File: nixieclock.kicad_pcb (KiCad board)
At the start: 2 copper layers, 33 parts, among them Q1 MMBTA42, Q2 FDS2672CT, U1 UCC3803

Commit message: things happened
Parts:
- added NX1: IN-12A, nixies-us:nixies-us-IN-12, F.Cu at (136.7, 42.7)
- added NX2: IN-12A, nixies-us:nixies-us-IN-12, F.Cu at (156.5, 42.2)
- added NX3: IN-12A, nixies-us:nixies-us-IN-12, F.Cu at (176.5, 42.0)
- added NX4: IN-12A, nixies-us:nixies-us-IN-12, F.Cu at (196.7, 42.0)
- added NX5: IN-12A, nixies-us:nixies-us-IN-12, F.Cu at (216.6, 42.0)
- added NX6: IN-12A, nixies-us:nixies-us-IN-12, F.Cu at (236.6, 42.0)
- moved Q1 50.8 mm to (168.4, 92.7)
- moved L2 50.0 mm to (159.7, 71.3)
- moved R3 49.8 mm to (144.9, 75.0)
- moved R4 49.8 mm to (144.9, 77.5)
- moved R5 49.8 mm to (144.9, 80.0)
- moved R7 49.8 mm to (144.9, 82.5)
- moved R8 49.8 mm to (144.9, 85.0)
- moved C10 49.8 mm to (136.0, 81.2)
- moved C13 49.8 mm to (136.0, 84.2)
- moved C14 49.8 mm to (136.0, 87.2)
- moved C2 49.8 mm to (130.6, 80.1)
- moved C5 49.8 mm to (136.0, 75.2)
- moved C7 49.8 mm to (130.6, 84.3)
- moved C9 49.8 mm to (136.0, 78.2)
- moved D2 49.8 mm to (173.2, 75.0)
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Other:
- board outline added: 135 x 79.8 mm
- copper layers 2 -> 11

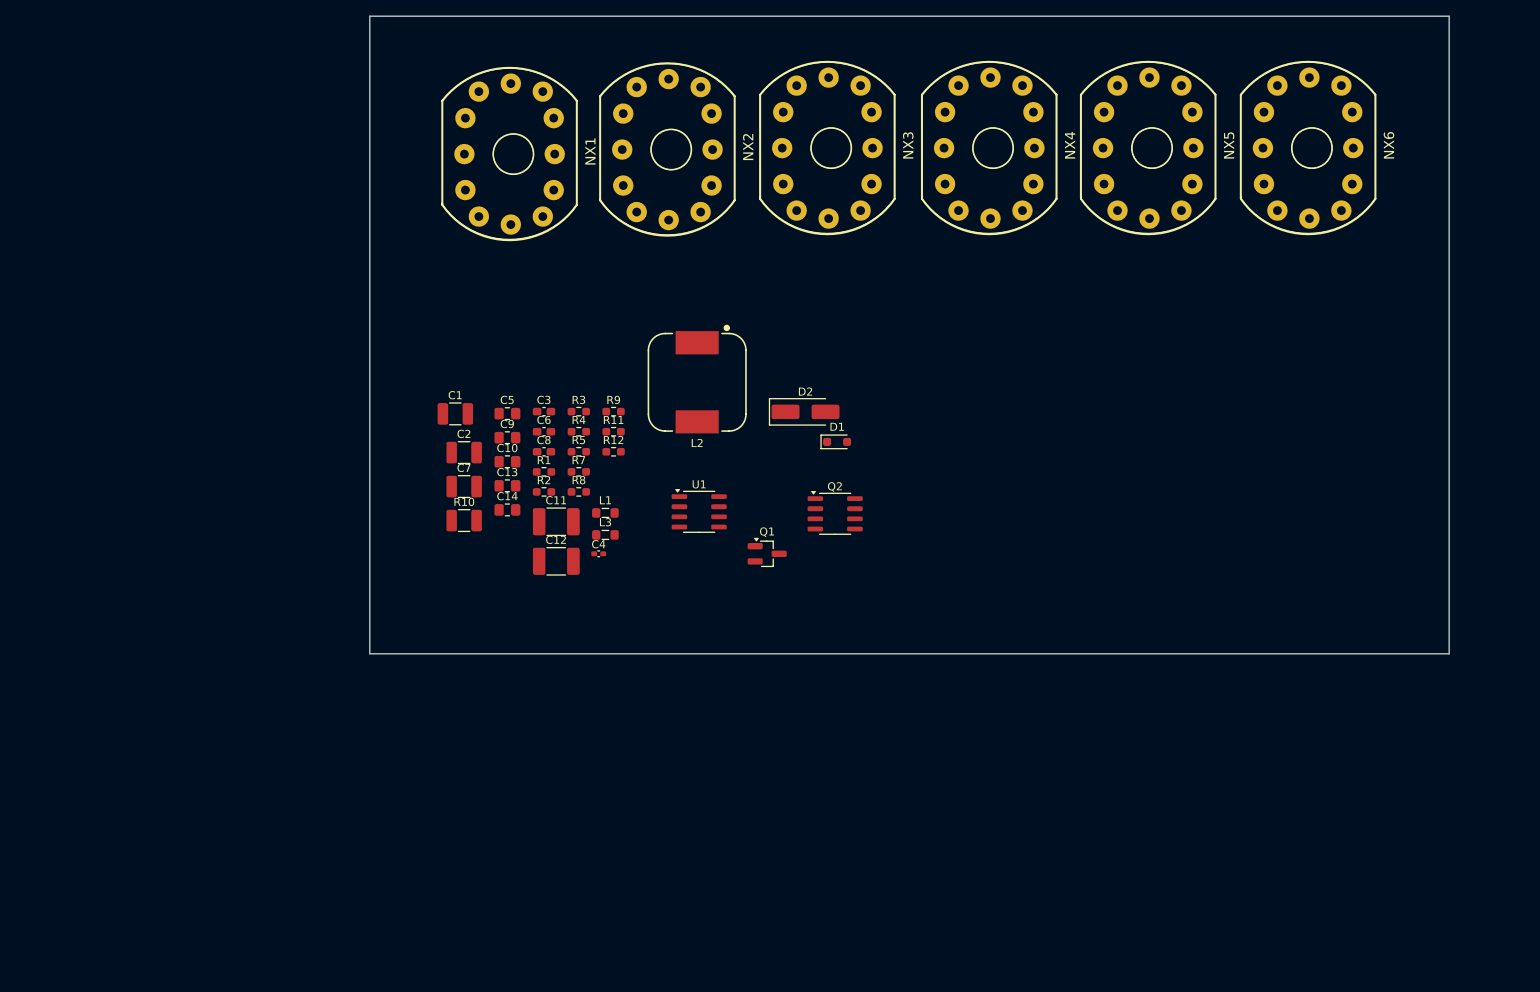
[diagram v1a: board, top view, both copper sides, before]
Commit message: schematic mostly done, started laying out board
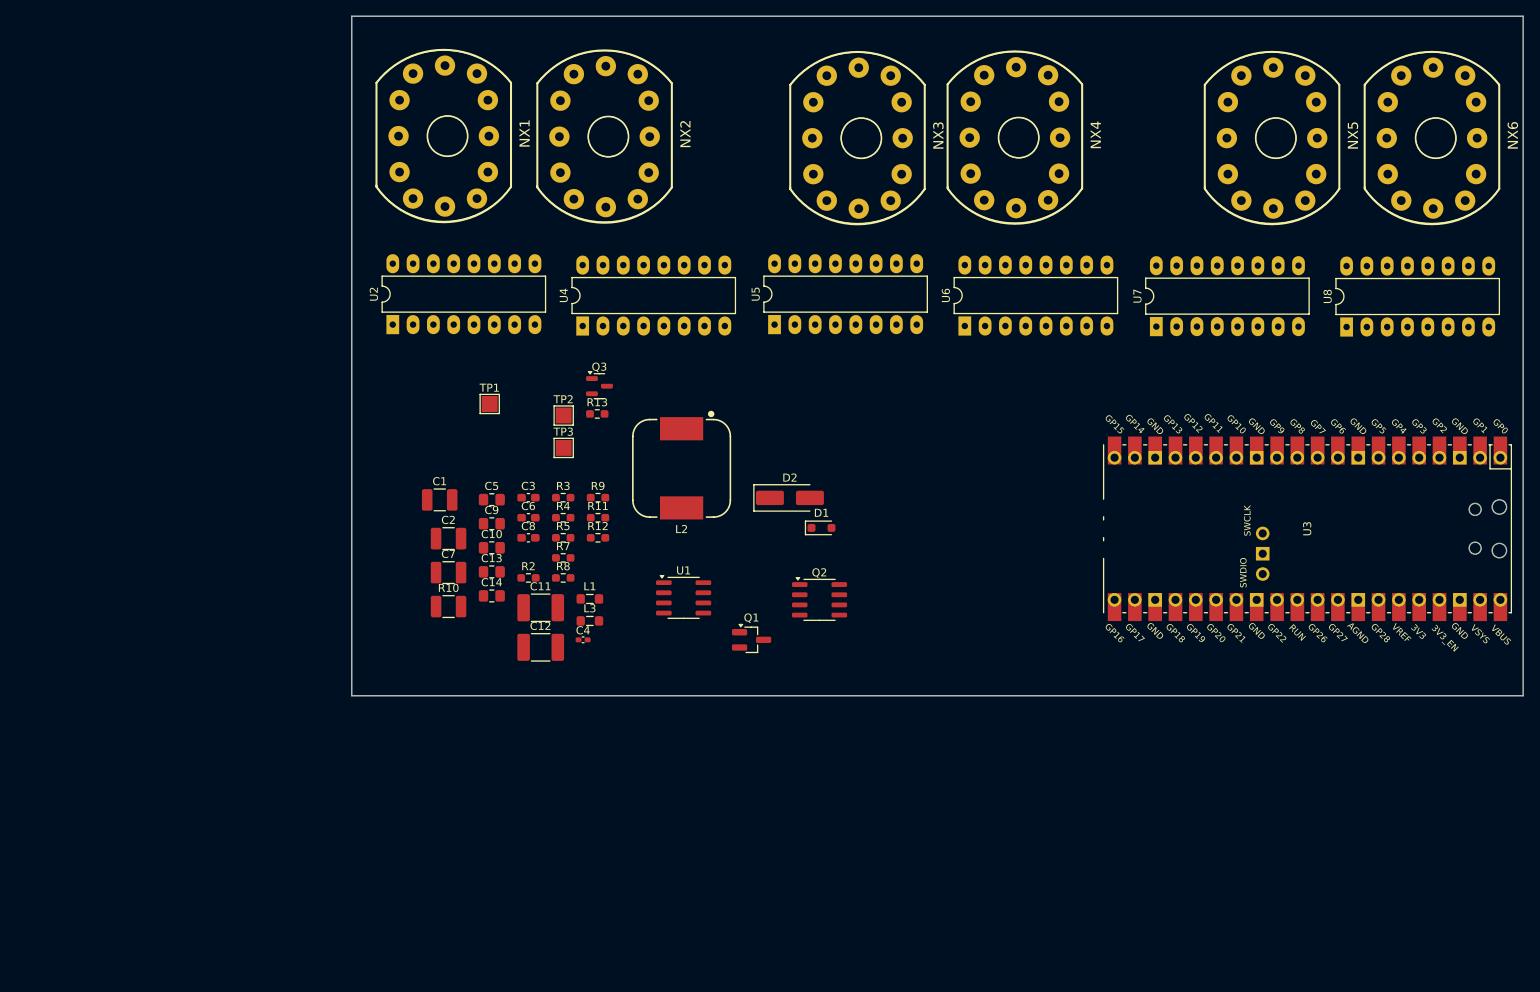
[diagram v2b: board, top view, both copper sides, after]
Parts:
- removed R1: 1k, Resistor_SMD:R_0603_1608Metric_Pad0.98x0.95mm_HandSolder
- added Q3: SS8050, Package_TO_SOT_SMD:SOT-23, F.Cu at (147.5, 71.8)
- added R13: 1k, Resistor_SMD:R_0603_1608Metric_Pad0.98x0.95mm_HandSolder, F.Cu at (147.2, 75.2)
- added TP1: TestPoint_Probe, TestPoint:TestPoint_Pad_2.0x2.0mm, F.Cu at (133.8, 74.0)
- added TP2: TestPoint_Probe, TestPoint:TestPoint_Pad_2.0x2.0mm, F.Cu at (143.0, 75.5)
- added TP3: TestPoint_Probe, TestPoint:TestPoint_Pad_2.0x2.0mm, F.Cu at (143.0, 79.5)
- added U2: K155NA1, Package_DIP:DIP-16_W7.62mm_LongPads, F.Cu at (121.6, 64.1)
- added U3: PicoW, RPi_Pico:RPi_PicoW_SMD_TH, F.Cu at (236.0, 89.6)
- added U4: K155NA1, Package_DIP:DIP-16_W7.62mm_LongPads, F.Cu at (145.4, 64.2)
- added U5: K155NA1, Package_DIP:DIP-16_W7.62mm_LongPads, F.Cu at (169.4, 64.1)
- added U6: K155NA1, Package_DIP:DIP-16_W7.62mm_LongPads, F.Cu at (193.2, 64.2)
- added U7: K155NA1, Package_DIP:DIP-16_W7.62mm_LongPads, F.Cu at (217.1, 64.3)
- added U8: K155NA1, Package_DIP:DIP-16_W7.62mm_LongPads, F.Cu at (240.9, 64.4)
- moved NX5 15.5 mm to (232.1, 40.8)
- moved NX6 15.5 mm to (252.1, 40.8)
- moved C13 10.9 mm to (134.0, 95.0)
- moved C14 10.9 mm to (134.0, 98.0)
- moved C2 10.9 mm to (128.6, 90.8)
- moved C5 10.9 mm to (134.0, 86.0)
- moved C7 10.9 mm to (128.6, 95.1)
- moved C9 10.9 mm to (134.0, 89.0)
- moved R10 10.9 mm to (128.6, 99.3)
- moved R11 10.9 mm to (147.3, 88.2)
- moved R3 10.9 mm to (142.9, 85.7)
- moved R4 10.9 mm to (142.9, 88.2)
- moved R7 10.9 mm to (142.9, 93.2)
- moved R8 10.9 mm to (142.9, 95.8)
- moved R9 10.9 mm to (147.3, 85.7)
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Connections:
- net +160V renamed +170V
- NX1 pad 0: unconnected-(NX1-Pad0) -> Net-(U2-0)
- NX1 pad 1: unconnected-(NX1-Pad1) -> Net-(U2-1)
- NX1 pad 2: unconnected-(NX1-Pad2) -> Net-(U2-2)
- NX1 pad 3: unconnected-(NX1-Pad3) -> Net-(U2-3)
- NX1 pad 4: unconnected-(NX1-Pad4) -> Net-(U2-4)
- NX1 pad 5: unconnected-(NX1-Pad5) -> Net-(U2-5)
- NX1 pad 6: unconnected-(NX1-Pad6) -> Net-(U2-6)
- NX1 pad 7: unconnected-(NX1-Pad7) -> Net-(U2-7)
- NX1 pad 8: unconnected-(NX1-Pad8) -> Net-(U2-8)
- NX1 pad 9: unconnected-(NX1-Pad9) -> Net-(U2-9)
- NX2 pad 0: unconnected-(NX2-Pad0) -> Net-(U4-0)
- NX2 pad 1: unconnected-(NX2-Pad1) -> Net-(U4-1)
- NX2 pad 2: unconnected-(NX2-Pad2) -> Net-(U4-2)
- NX2 pad 3: unconnected-(NX2-Pad3) -> Net-(U4-3)
- NX2 pad 4: unconnected-(NX2-Pad4) -> Net-(U4-4)
- NX2 pad 5: unconnected-(NX2-Pad5) -> Net-(U4-5)
- NX2 pad 6: unconnected-(NX2-Pad6) -> Net-(U4-6)
- NX2 pad 7: unconnected-(NX2-Pad7) -> Net-(U4-7)
- NX2 pad 8: unconnected-(NX2-Pad8) -> Net-(U4-8)
- NX2 pad 9: unconnected-(NX2-Pad9) -> Net-(U4-9)
- NX3 pad 0: unconnected-(NX3-Pad0) -> Net-(U5-0)
- NX3 pad 1: unconnected-(NX3-Pad1) -> Net-(U5-1)
- NX3 pad 2: unconnected-(NX3-Pad2) -> Net-(U5-2)
- NX3 pad 3: unconnected-(NX3-Pad3) -> Net-(U5-3)
- NX3 pad 4: unconnected-(NX3-Pad4) -> Net-(U5-4)
- NX3 pad 5: unconnected-(NX3-Pad5) -> Net-(U5-5)
- NX3 pad 6: unconnected-(NX3-Pad6) -> Net-(U5-6)
- NX3 pad 7: unconnected-(NX3-Pad7) -> Net-(U5-7)
- NX3 pad 8: unconnected-(NX3-Pad8) -> Net-(U5-8)
- NX3 pad 9: unconnected-(NX3-Pad9) -> Net-(U5-9)
- NX4 pad 0: unconnected-(NX4-Pad0) -> Net-(U6-0)
- NX4 pad 1: unconnected-(NX4-Pad1) -> Net-(U6-1)
- NX4 pad 2: unconnected-(NX4-Pad2) -> Net-(U6-2)
- NX4 pad 3: unconnected-(NX4-Pad3) -> Net-(U6-3)
- NX4 pad 4: unconnected-(NX4-Pad4) -> Net-(U6-4)
- NX4 pad 5: unconnected-(NX4-Pad5) -> Net-(U6-5)
- NX4 pad 6: unconnected-(NX4-Pad6) -> Net-(U6-6)
- NX4 pad 7: unconnected-(NX4-Pad7) -> Net-(U6-7)
- NX4 pad 8: unconnected-(NX4-Pad8) -> Net-(U6-8)
- NX4 pad 9: unconnected-(NX4-Pad9) -> Net-(U6-9)
- NX5 pad 0: unconnected-(NX5-Pad0) -> Net-(U7-0)
- NX5 pad 1: unconnected-(NX5-Pad1) -> Net-(U7-1)
- NX5 pad 2: unconnected-(NX5-Pad2) -> Net-(U7-2)
- NX5 pad 3: unconnected-(NX5-Pad3) -> Net-(U7-3)
- NX5 pad 4: unconnected-(NX5-Pad4) -> Net-(U7-4)
- NX5 pad 5: unconnected-(NX5-Pad5) -> Net-(U7-5)
- NX5 pad 6: unconnected-(NX5-Pad6) -> Net-(U7-6)
- NX5 pad 7: unconnected-(NX5-Pad7) -> Net-(U7-7)
- NX5 pad 8: unconnected-(NX5-Pad8) -> Net-(U7-8)
- NX5 pad 9: unconnected-(NX5-Pad9) -> Net-(U7-9)
- NX6 pad 0: unconnected-(NX6-Pad0) -> Net-(U8-0)
- NX6 pad 1: unconnected-(NX6-Pad1) -> Net-(U8-1)
- NX6 pad 2: unconnected-(NX6-Pad2) -> Net-(U8-2)
- NX6 pad 3: unconnected-(NX6-Pad3) -> Net-(U8-3)
- NX6 pad 4: unconnected-(NX6-Pad4) -> Net-(U8-4)
- NX6 pad 5: unconnected-(NX6-Pad5) -> Net-(U8-5)
- NX6 pad 6: unconnected-(NX6-Pad6) -> Net-(U8-6)
- NX6 pad 7: unconnected-(NX6-Pad7) -> Net-(U8-7)
- NX6 pad 8: unconnected-(NX6-Pad8) -> Net-(U8-8)
- NX6 pad 9: unconnected-(NX6-Pad9) -> Net-(U8-9)
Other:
- board size 135 x 79.8 mm -> 146.5 x 85 mm

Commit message: layout
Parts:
- moved D1 42.3 mm to (133.0, 90.0)
- moved Q3 37.1 mm to (129.9, 104.5)
- moved Q1 37.1 mm to (129.8, 98.8), turned to 180 degrees
- moved R13 34.8 mm to (125.5, 102.5), turned to 180 degrees
- moved C11 33.3 mm to (171.8, 89.0), turned to 90 degrees
- moved C13 31.9 mm to (165.8, 98.5), turned to -90 degrees
- moved C12 31.8 mm to (170.8, 96.0), turned to -90 degrees
- moved C9 28.5 mm to (162.5, 89.8)
- moved C7 28.1 mm to (153.2, 81.6), turned to 90 degrees
- moved R10 26.5 mm to (155.0, 96.8), turned to -90 degrees
- moved C10 26.5 mm to (160.2, 95.5), turned to 90 degrees
- moved C14 25.2 mm to (159.0, 101.0), turned to -90 degrees
- moved TP2 23.2 mm to (120.2, 70.7)
- moved TP3 23.2 mm to (120.2, 75.0)
- moved Q2 20.8 mm to (156.2, 89.5), turned to 90 degrees
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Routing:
- net Net-(U1-FB): track 0.00 -> 41.9 mm
- net Net-(D2-A): track 0.00 -> 41.3 mm
- net Net-(U1-Isense): track 0.00 -> 29.0 mm
- net Net-(D2-K): track 0.00 -> 26.1 mm
- net Net-(U1-Vcc): track 0.00 -> 26.0 mm, vias 0 -> 2
- net +5V: track 0.00 -> 18.9 mm
- net Net-(D1-K): track 0.00 -> 15.9 mm
- net Net-(D1-A): track 0.00 -> 15.4 mm
- net Net-(Q2-G): track 0.00 -> 15.2 mm, vias 0 -> 2
- net Net-(U1-Vref): track 0.00 -> 14.3 mm
- net Net-(Q2-S-Pad1): track 0.00 -> 12.2 mm
- net Net-(Q1-B): track 0.00 -> 11.1 mm
- net Net-(U1-R/C): track 0.00 -> 5.63 mm
- net +170V: track 0.00 -> 3.88 mm
- net Net-(Q3-B): track 0.00 -> 3.00 mm
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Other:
- board text added: "+170V"
- board text added: "+5V"
- board text added: "GND"

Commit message: mostly done i guess?
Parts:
- added R1: 10.5k, Resistor_SMD:R_0805_2012Metric_Pad1.20x1.40mm_HandSolder, F.Cu at (100.3, 59.5)
- added R14: 10.5k, Resistor_SMD:R_0805_2012Metric_Pad1.20x1.40mm_HandSolder, F.Cu at (120.1, 59.8)
- added R15: 10.5k, Resistor_SMD:R_0805_2012Metric_Pad1.20x1.40mm_HandSolder, F.Cu at (151.6, 59.8)
- added R16: 10.5k, Resistor_SMD:R_0805_2012Metric_Pad1.20x1.40mm_HandSolder, F.Cu at (171.3, 59.8)
- added R17: 10.5k, Resistor_SMD:R_0805_2012Metric_Pad1.20x1.40mm_HandSolder, F.Cu at (203.3, 60.0)
- added R18: 10.5k, Resistor_SMD:R_0805_2012Metric_Pad1.20x1.40mm_HandSolder, F.Cu at (222.3, 60.0)
- R11, R12: footprint Resistor_SMD:R_0603_1608Metric_Pad0.98x0.95mm_HandSolder -> Resistor_SMD:R_1206_3216Metric_Pad1.30x1.75mm_HandSolder
- moved U3 50.6 mm to (197.2, 118.7)
- moved U4 50.3 mm to (105.2, 94.6)
- moved C1 50.3 mm to (90.1, 125.7)
- moved C10 50.3 mm to (121.3, 127.4)
- moved C2 50.3 mm to (85.3, 121.9)
- moved C3 50.3 mm to (81.6, 121.6)
- moved C6 50.3 mm to (110.3, 129.8)
- moved C7 50.3 mm to (114.3, 113.5)
- moved C9 50.3 mm to (123.6, 121.7)
- moved D1 50.3 mm to (94.1, 121.9)
- moved D2 50.3 mm to (125.6, 116.9)
- moved L1 50.3 mm to (118.1, 113.9)
- moved L2 50.3 mm to (104.1, 118.2)
- moved Q2 50.3 mm to (117.3, 121.4)
- moved Q3 50.3 mm to (91.0, 136.4)
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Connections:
- NX1 pad A: unconnected-(NX1-PadA) -> Net-(NX1-PadA)
- NX2 pad A: unconnected-(NX2-PadA) -> Net-(NX2-PadA)
- NX3 pad A: unconnected-(NX3-PadA) -> Net-(NX3-PadA)
- NX4 pad A: unconnected-(NX4-PadA) -> Net-(NX4-PadA)
- NX5 pad A: unconnected-(NX5-PadA) -> Net-(NX5-PadA)
- NX6 pad A: unconnected-(NX6-PadA) -> Net-(NX6-PadA)
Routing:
- net +170V: track 3.88 -> 281.0 mm
- net +5V: track 18.9 -> 258.2 mm, vias 0 -> 1
- net GPIO0: track 0.00 -> 169.0 mm, vias 0 -> 1
- net GPIO1: track 0.00 -> 146.7 mm, vias 0 -> 1
- net GPIO4: track 0.00 -> 131.1 mm
- net GPIO3: track 0.00 -> 129.7 mm, vias 0 -> 1
- net GPIO2: track 0.00 -> 129.6 mm, vias 0 -> 1
- net GPIO5: track 0.00 -> 111.0 mm, vias 0 -> 1
- net GPIO8: track 0.00 -> 101.3 mm, vias 0 -> 1
- net GPIO6: track 0.00 -> 95.7 mm, vias 0 -> 1
- net GPIO7: track 0.00 -> 90.9 mm, vias 0 -> 1
- net GPIO9: track 0.00 -> 72.5 mm, vias 0 -> 1
- net GPIO12: track 0.00 -> 59.6 mm, vias 0 -> 1
- net GPIO10: track 0.00 -> 56.0 mm, vias 0 -> 1
- net GPIO11: track 0.00 -> 53.5 mm, vias 0 -> 1
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- added copper zone on F.Cu, net GND
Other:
- board text added: "Designed by Alex Park"
- board text added: "High Voltage"
- board text added: "Warning"

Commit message: Finishing touches to pcb
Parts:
- R18: value 10.5k -> R18
- moved Q3 1.86 mm to (91.2, 134.6)
- moved C3 1.16 mm to (82.8, 121.5)
- moved C8 1.01 mm to (98.0, 132.0)
- moved R8 1.01 mm to (105.0, 135.2)
- moved C10 0.85 mm to (120.5, 127.4)
- moved C11 0.79 mm to (133.5, 120.5)
- moved NX1 0.52 mm to (91.0, 71.3)
- moved NX5 0.42 mm to (193.8, 71.3)
- moved NX6 0.42 mm to (213.8, 71.3)
- moved NX2 0.36 mm to (111.0, 71.3)
- moved NX4 0.25 mm to (162.2, 71.3)
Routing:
- net GND: track 0.00 -> 61.5 mm, vias 0 -> 9
- net Net-(U4-4): track 44.8 -> 28.2 mm
- net Net-(D2-K): track 28.6 -> 36.6 mm
- net Net-(U5-7): track 33.7 -> 25.9 mm
- net Net-(U6-5): track 24.6 -> 31.4 mm, vias 0 -> 1
- net Net-(U4-8): track 32.9 -> 39.6 mm, vias 0 -> 1
- net Net-(U5-9): track 40.0 -> 33.3 mm, vias 1 -> 0
- net Net-(U8-2): track 36.6 -> 30.0 mm
- net Net-(U5-4): track 29.6 -> 23.0 mm
- net Net-(U6-2): track 33.2 -> 39.5 mm
- net Net-(U8-4): track 22.0 -> 28.2 mm
- net Net-(U4-0): track 18.2 -> 24.2 mm
- net Net-(U5-8): track 49.5 -> 43.5 mm, vias 0 -> 1
- net Net-(U8-1): track 9.30 -> 15.2 mm
- net Net-(U8-7): track 31.6 -> 25.8 mm
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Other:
- copper layers 11 -> 2
